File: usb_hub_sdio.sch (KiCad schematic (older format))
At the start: 18 parts, among them U901 USB2660, Y901 24MHz

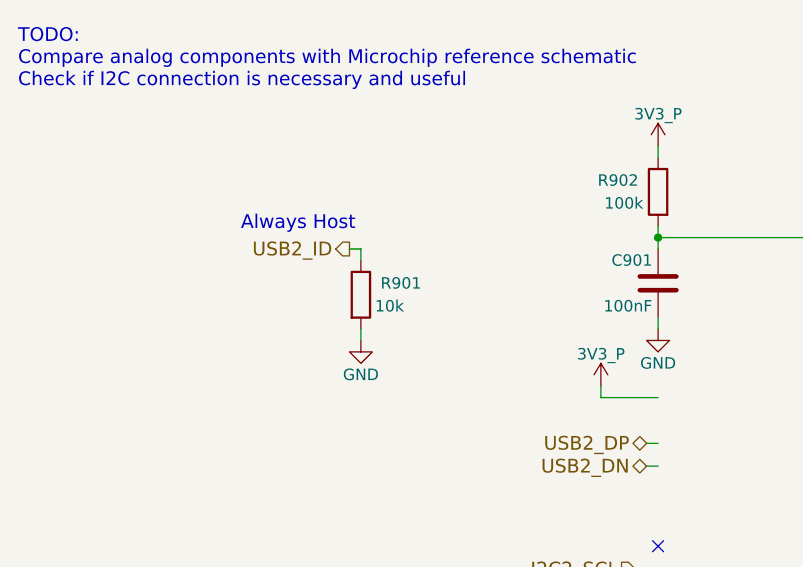
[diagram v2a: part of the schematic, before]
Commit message: Begin assigning footprints to passive components, add component information to the common 10k resistors throughout the schematic, include TVS diodes on the switch/button I/O pins, use the DB2J20900L schottky diode throughout the design (in place of the ZLLS400)
Added notes about the battery holder, battery size, and the fact that the 103HT thermistor can fit underneath the 18650 battery when the battery is insterted into the holder.

Included frequency response curve for the new/cheaper SMD speaker (slightly thicker mechanical dimension).

Included note about the RedPine RS9116's SDIO_RESET# line expecting a 2.31V VIH logic level, increased the pull-up to 100k (M.2 standard states that this is should be 1.8V level).

Added a TODO note stating the 1.8V logic-level I2C devices should share the same level-shifter that will be on the top-level circuit (in next commit).
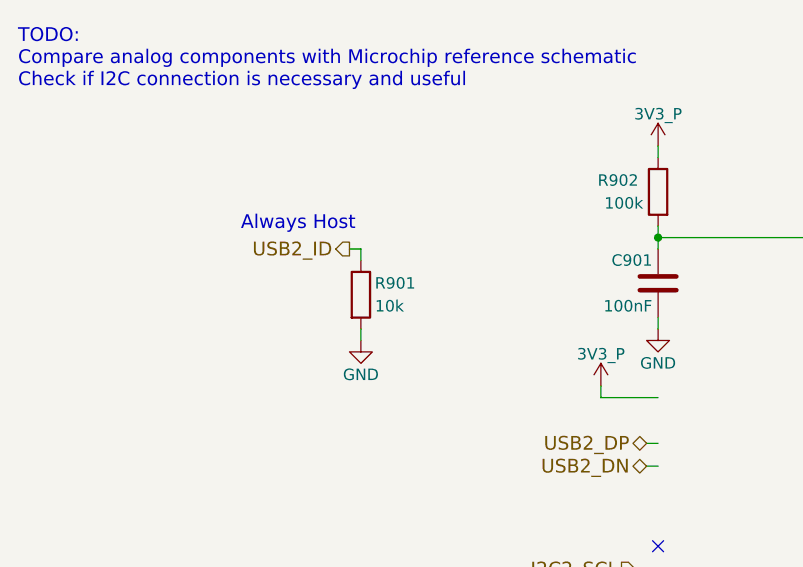
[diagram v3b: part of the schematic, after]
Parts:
- R901: footprint (none) -> Resistors_SMD:R_0603; Distrib Link (none) -> https://www.digikey.com/product-detail/en/stackpole-electro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; Distrib PN (none) -> RMCF0603JG10K0CT-ND; MFG Name (none) -> Stackpole; MFG Part Num (none) -> RMCF0603JG10K0; Others (none) -> https://www.digikey.com/products/en/resistors/chip-resistor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; Tolerance (none) -> 5%
- R902, R903: footprint (none) -> Resistors_SMD:R_0603
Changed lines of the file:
@@
 F 0 "R903" H 5075 5950 50  0000 C CNN
 F 1 "12k" H 5025 6050 50  0000 C CNN
-F 2 "" V 4830 6000 50  0001 C CNN
+F 2 "Resistors_SMD:R_0603" V 4830 6000 50  0001 C CNN
 F 3 "" H 4900 6000 50  0001 C CNN
 	1    4900 6000
@@
 $EndComp
 $Comp
-L GND #PWR905
+L GND #PWR0138
 U 1 1 5AFD409A
 P 4250 6550
-F 0 "#PWR905" H 4250 6300 50  0001 C CNN
+F 0 "#PWR0138" H 4250 6300 50  0001 C CNN
 F 1 "GND" H 4250 6400 50  0000 C CNN
 F 2 "" H 4250 6550 50  0001 C CNN
@@
 $EndComp
 $Comp
-L GND #PWR906
+L GND #PWR0139
 U 1 1 5AFD422F
 P 4650 6550
-F 0 "#PWR906" H 4650 6300 50  0001 C CNN
+F 0 "#PWR0139" H 4650 6300 50  0001 C CNN
 F 1 "GND" H 4650 6400 50  0000 C CNN
 F 2 "" H 4650 6550 50  0001 C CNN
@@
 F 0 "R902" H 4075 1700 50  0000 C CNN
 F 1 "100k" H 4050 1600 50  0000 C CNN
-F 2 "" V 3830 1650 50  0001 C CNN
+F 2 "Resistors_SMD:R_0603" V 3830 1650 50  0001 C CNN
 F 3 "" H 3900 1650 50  0001 C CNN
 	1    3900 1650
@@
 $EndComp
 $Comp
-L GND #PWR904
+L GND #PWR0140
 U 1 1 5AE5E881
 P 3900 2250
-F 0 "#PWR904" H 3900 2000 50  0001 C CNN
+F 0 "#PWR0140" H 3900 2000 50  0001 C CNN
 F 1 "GND" H 3900 2100 50  0000 C CNN
 F 2 "" H 3900 2250 50  0001 C CNN
@@
 $EndComp
 $Comp
-L 3V3_P #PWR903
+L 3V3_P #PWR0141
 U 1 1 5AE604F2
 P 3900 1450
-F 0 "#PWR903" H 3900 1300 50  0001 C CNN
+F 0 "#PWR0141" H 3900 1300 50  0001 C CNN
 F 1 "3V3_P" H 3900 1590 50  0000 C CNN
 F 2 "" H 3900 1450 50  0001 C CNN
@@
 USB2_ID
 $Comp
-L R R901
-U 1 1 5AF23335
-P 2600 2100
-F 0 "R901" H 2775 2150 50  0000 C CNN
-F 1 "10k" H 2725 2050 50  0000 C CNN
-F 2 "" V 2530 2100 50  0001 C CNN
-F 3 "" H 2600 2100 50  0001 C CNN
-	1    2600 2100
-	1    0    0    -1
-$EndComp
-$Comp
-L GND #PWR901
+L GND #PWR0142
 U 1 1 5AF52101
 P 2600 2300
-F 0 "#PWR901" H 2600 2050 50  0001 C CNN
+F 0 "#PWR0142" H 2600 2050 50  0001 C CNN
 F 1 "GND" H 2600 2150 50  0000 C CNN
 F 2 "" H 2600 2300 50  0001 C CNN
@@
 $EndComp
 $Comp
-L GND #PWR908
+L GND #PWR0143
 U 1 1 5B0063B4
 P 4900 6200
-F 0 "#PWR908" H 4900 5950 50  0001 C CNN
+F 0 "#PWR0143" H 4900 5950 50  0001 C CNN
 F 1 "GND" H 4900 6050 50  0000 C CNN
 F 2 "" H 4900 6200 50  0001 C CNN
@@
 $EndComp
 $Comp
-L GND #PWR910
+L GND #PWR0144
 U 1 1 5B00652F
 P 6300 5900
-F 0 "#PWR910" H 6300 5650 50  0001 C CNN
+F 0 "#PWR0144" H 6300 5650 50  0001 C CNN
 F 1 "GND" H 6300 5750 50  0000 C CNN
 F 2 "" H 6300 5900 50  0001 C CNN
@@
 NoConn ~ 3900 3500
 $Comp
-L 3V3_P #PWR909
+L 3V3_P #PWR0145
 U 1 1 5B00782B
 P 5700 950
-F 0 "#PWR909" H 5700 800 50  0001 C CNN
+F 0 "#PWR0145" H 5700 800 50  0001 C CNN
 F 1 "3V3_P" H 5700 1090 50  0000 C CNN
 F 2 "" H 5700 950 50  0001 C CNN
@@
 $EndComp
 $Comp
-L GND #PWR907
+L GND #PWR0146
 U 1 1 5B008B68
 P 4700 1450
-F 0 "#PWR907" H 4700 1200 50  0001 C CNN
+F 0 "#PWR0146" H 4700 1200 50  0001 C CNN
 F 1 "GND" H 4700 1300 50  0000 C CNN
 F 2 "" H 4700 1450 50  0001 C CNN
@@
 $EndComp
 $Comp
-L GND #PWR912
+L GND #PWR0147
 U 1 1 5B00B145
 P 7600 2150
-F 0 "#PWR912" H 7600 1900 50  0001 C CNN
+F 0 "#PWR0147" H 7600 1900 50  0001 C CNN
 F 1 "GND" H 7600 2000 50  0000 C CNN
 F 2 "" H 7600 2150 50  0001 C CNN
@@
 $EndComp
 $Comp
-L GND #PWR911
+L GND #PWR0148
 U 1 1 5B00BA9D
 P 7600 1450
-F 0 "#PWR911" H 7600 1200 50  0001 C CNN
+F 0 "#PWR0148" H 7600 1200 50  0001 C CNN
 F 1 "GND" H 7600 1300 50  0000 C CNN
 F 2 "" H 7600 1450 50  0001 C CNN
@@
 uSD_DATA3
 $Comp
-L 3V3_P #PWR902
+L 3V3_P #PWR0149
 U 1 1 5B00E09B
 P 3650 2500
-F 0 "#PWR902" H 3650 2350 50  0001 C CNN
+F 0 "#PWR0149" H 3650 2350 50  0001 C CNN
 F 1 "3V3_P" H 3650 2640 50  0000 C CNN
 F 2 "" H 3650 2500 50  0001 C CNN
@@
 	5200 1350 5200 1400
 Connection ~ 4700 1400
+$Comp
+L R R901
+U 1 1 5B31F267
+P 2600 2100
+F 0 "R901" H 2750 2150 50  0000 C CNN
+F 1 "10k" H 2725 2050 50  0000 C CNN
+F 2 "Resistors_SMD:R_0603" V 2530 2100 50  0001 C CNN
+F 3 "https://www.seielect.com/Catalog/SEI-RMCF_RMCP.pdf" H 2600 2100 50  0001 C CNN
+F 4 "Stackpole" H 2600 2100 60  0001 C CNN "MFG Name"
+F 5 "RMCF0603JG10K0" H 2600 2100 60  0001 C CNN "MFG Part Num"
+F 6 "RMCF0603JG10K0CT-ND" H 2600 2100 60  0001 C CNN "Distrib PN"
+F 7 "https://www.digikey.com/product-detail/en/stackpole-electronics-inc/RMCF0603JG10K0/RMCF0603JG10K0CT-ND/4425128" H 2600 2100 60  0001 C CNN "Distrib Link"
+F 8 "5%" H 2600 2100 60  0001 C CNN "Tolerance"
+F 9 "https://www.digikey.com/products/en/resistors/chip-resistor-surface-mount/52?FV=ffe00034%2C400005%2C1f140000%2Cmu10+kOhms%7C2085&quantity=&ColumnSort=1000011&page=1&pageSize=500" H 2600 2100 60  0001 C CNN "Others"
+	1    2600 2100
+	1    0    0    -1
+$EndComp
 $EndSCHEMATC

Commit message: Move MIPI DSI & CSI sheets into a "MIPI" sheet, both DSI and CSI will likely use the I2C level shifter
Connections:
- net labels added: I2C1_SCL, I2C1_SDA
- net labels removed: I2C2_SCL, I2C2_SDA
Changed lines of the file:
@@
 $Descr A4 11693 8268
 encoding utf-8
-Sheet 9 21
+Sheet 9 22
 Title ""
 Date "2018-05-18"
@@
 USB2_DP
 Text HLabel 3800 3300 0    60   Input ~ 0
-I2C2_SCL
+I2C1_SCL
 Text HLabel 3800 3400 0    60   BiDi ~ 0
-I2C2_SDA
+I2C1_SDA
 Text HLabel 2550 1900 0    60   Output ~ 0
 USB2_ID

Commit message: Add Prolific MA8627 USB hub + SDIO bridge chip and use it in place of the USB2660, SD interface used with the uSD (not WLAN)
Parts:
- removed U901: USB2660, symbol USB2660
- added Q901: DMG2301L, symbol Q_PMOS_GSD
- added R904, R905: 0, Resistors_SMD:R_0603, symbol R
- added R906: 10k, symbol R
- added R907: 330, Resistors_SMD:R_0603, symbol R
- added R908, R909, R910, R911: NC, Resistors_SMD:R_0603, symbol R
- added U901: MA8627, symbol MA8627
- C901: value 100nF -> 4.7uF
- C902, C903: value NC -> 18pF; footprint (none) -> Capacitors_SMD:C_0603
- C904: value 1uF -> 100nF
- C905: value 1nF -> 10uF; footprint (none) -> Resistors_SMD:R_0603
- C906, C907: value 4.7uF -> 10uF; footprint (none) -> Resistors_SMD:R_0603
- C908: value 1uF -> 10uF; footprint (none) -> Resistors_SMD:R_0603
- C909: footprint (none) -> Capacitors_SMD:C_0603
- C910, C911: value 1nF -> 10uF; footprint (none) -> Capacitors_SMD:C_0603
- C912: value 100nF -> NC; footprint (none) -> Capacitors_SMD:C_0603
- C913: value 100nF -> 10uF; footprint (none) -> Capacitors_SMD:C_0603
- R902: value 100k -> NC
- R903: value 12k -> 330
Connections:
- net labels added: 3V3_SD, 5V_P, CD, DM0, DP0, HV33, RDRV18, RDRV33, RDRV5, SDCD, SMARTCARD_DM, SMARTCARD_DP, SRST, WP
- net labels removed: 3V3_P, I2C1_SCL, I2C1_SDA
- wire segments 76 -> 116
- no-connect marks 32 -> 5
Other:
- note added: "Can be swapped arround depending on layout"
- note added: "TODO:\nShould be NC?"
- note added: "≤1%"
- note removed: "18pF"
- note removed: "TODO:\nCompare analog components with Microchip reference schematic\nCheck if I2C connection is necessary and useful"
- moved on the sheet: C902, C903, R901, Y901

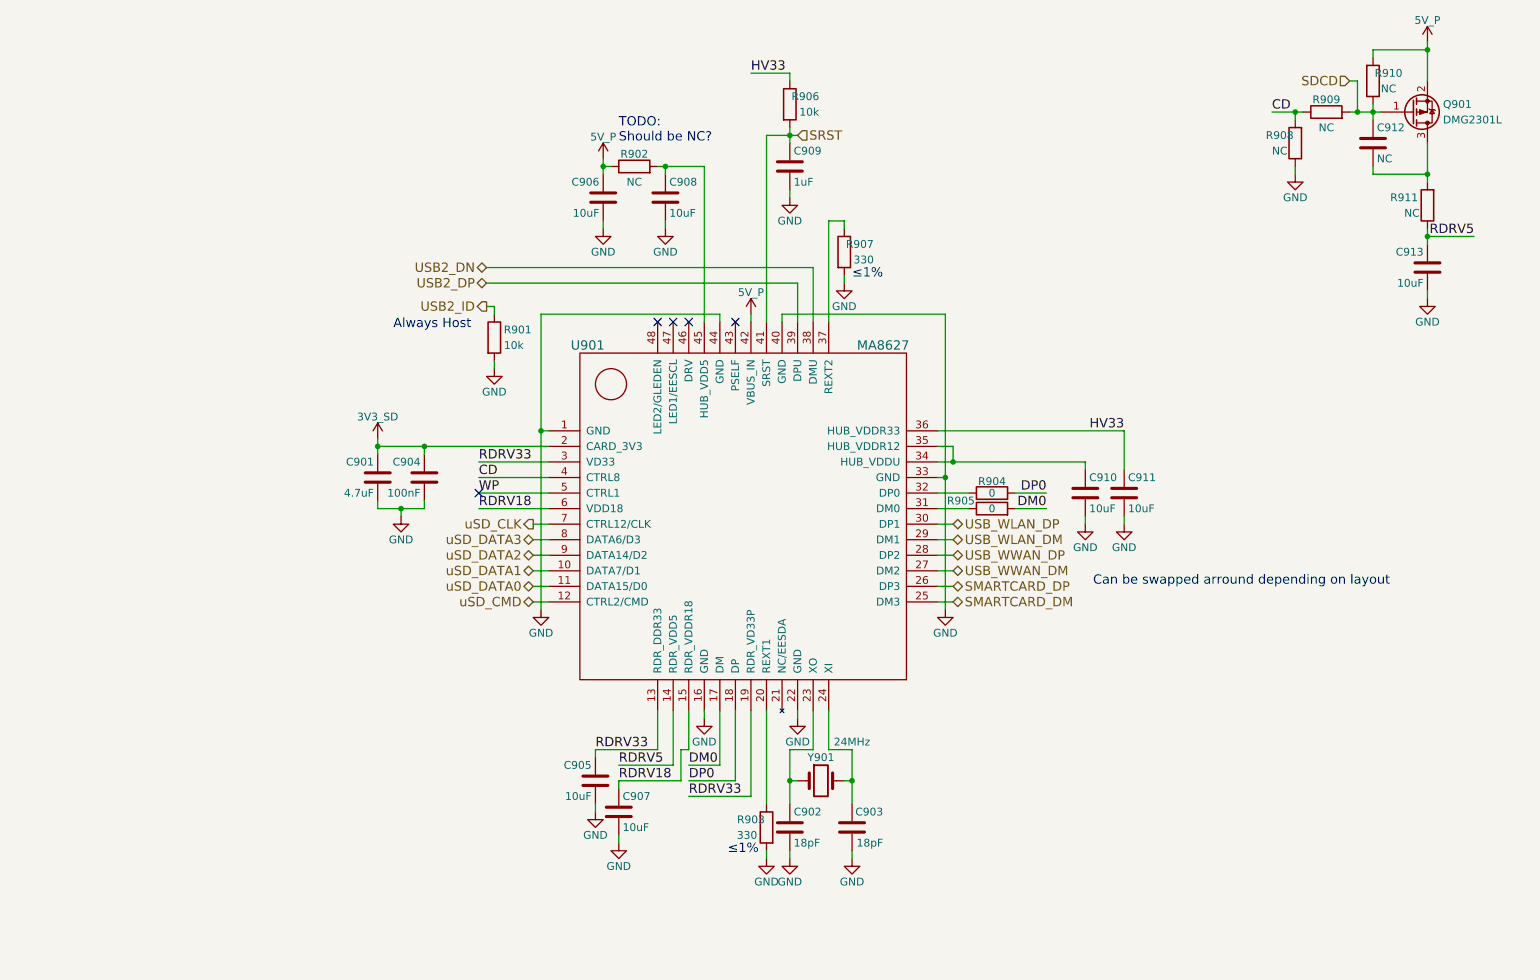
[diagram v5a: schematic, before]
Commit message: Add smart card circuit using the SEC1110 USB to ISO/IEC 7816 bridge chip, include ID-0001/2FF/mini-SIM socket connector selection informatino (1010027182)
Need to create footprint for the mini-SIM socket
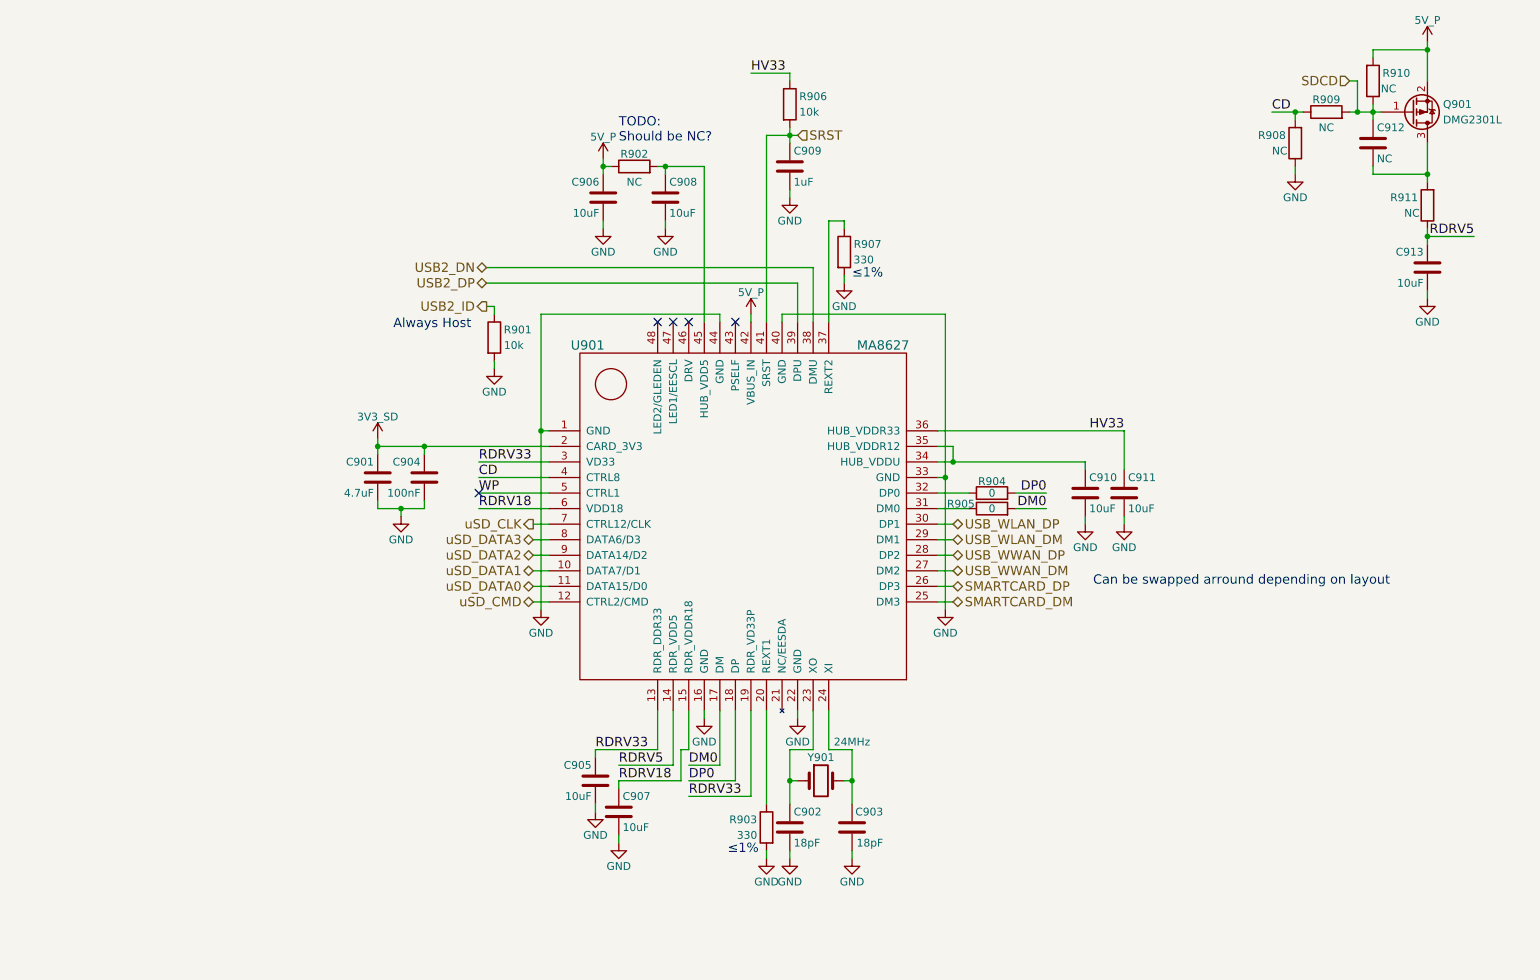
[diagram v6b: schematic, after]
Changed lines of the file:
@@
 $Descr A4 11693 8268
 encoding utf-8
-Sheet 9 22
+Sheet 9 23
 Title ""
-Date "2018-05-18"
+Date "2018-05-23"
 Rev "v0.1.0"
 Comp "Purism SPC"
@@
 U 1 1 5B07DA80
 P 7400 3800
-F 0 "R905" V 7450 4000 50  0000 C CNN
+F 0 "R905" V 7430 4000 50  0000 C CNN
 F 1 "0" V 7400 3800 50  0000 C CNN
 F 2 "Resistors_SMD:R_0603" V 7330 3800 50  0001 C CNN
@@
 U 1 1 5B09B6A4
 P 9350 1450
-F 0 "R908" H 9450 1400 50  0000 C CNN
+F 0 "R908" H 9500 1400 50  0000 C CNN
 F 1 "NC" H 9450 1500 50  0000 C CNN
 F 2 "Resistors_SMD:R_0603" V 9280 1450 50  0001 C CNN
@@
 U 1 1 5B09C779
 P 9850 1050
-F 0 "R910" H 9950 1000 50  0000 C CNN
+F 0 "R910" H 10000 1000 50  0000 C CNN
 F 1 "NC" H 9950 1100 50  0000 C CNN
 F 2 "Resistors_SMD:R_0603" V 9780 1050 50  0001 C CNN
@@
 U 1 1 5B0FC98F
 P 6100 1200
-F 0 "R906" H 6200 1250 50  0000 C CNN
+F 0 "R906" H 6250 1250 50  0000 C CNN
 F 1 "10k" H 6225 1150 50  0000 C CNN
 F 2 "" V 6030 1200 50  0001 C CNN
@@
 U 1 1 5B101B57
 P 5950 5850
-F 0 "R903" H 6050 5900 50  0000 C CNN
+F 0 "R903" H 6100 5900 50  0000 C CNN
 F 1 "330" H 6075 5800 50  0000 C CNN
 F 2 "Resistors_SMD:R_0603" V 5880 5850 50  0001 C CNN
@@
 U 1 1 5B10A19C
 P 6450 2150
-F 0 "R907" H 6550 2200 50  0000 C CNN
+F 0 "R907" H 6600 2200 50  0000 C CNN
 F 1 "330" H 6575 2100 50  0000 C CNN
 F 2 "Resistors_SMD:R_0603" V 6380 2150 50  0001 C CNN

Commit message: Make changes to the USB hub + SD bridge circuit and uSD sheet based on Prolific's feedback after asking questions
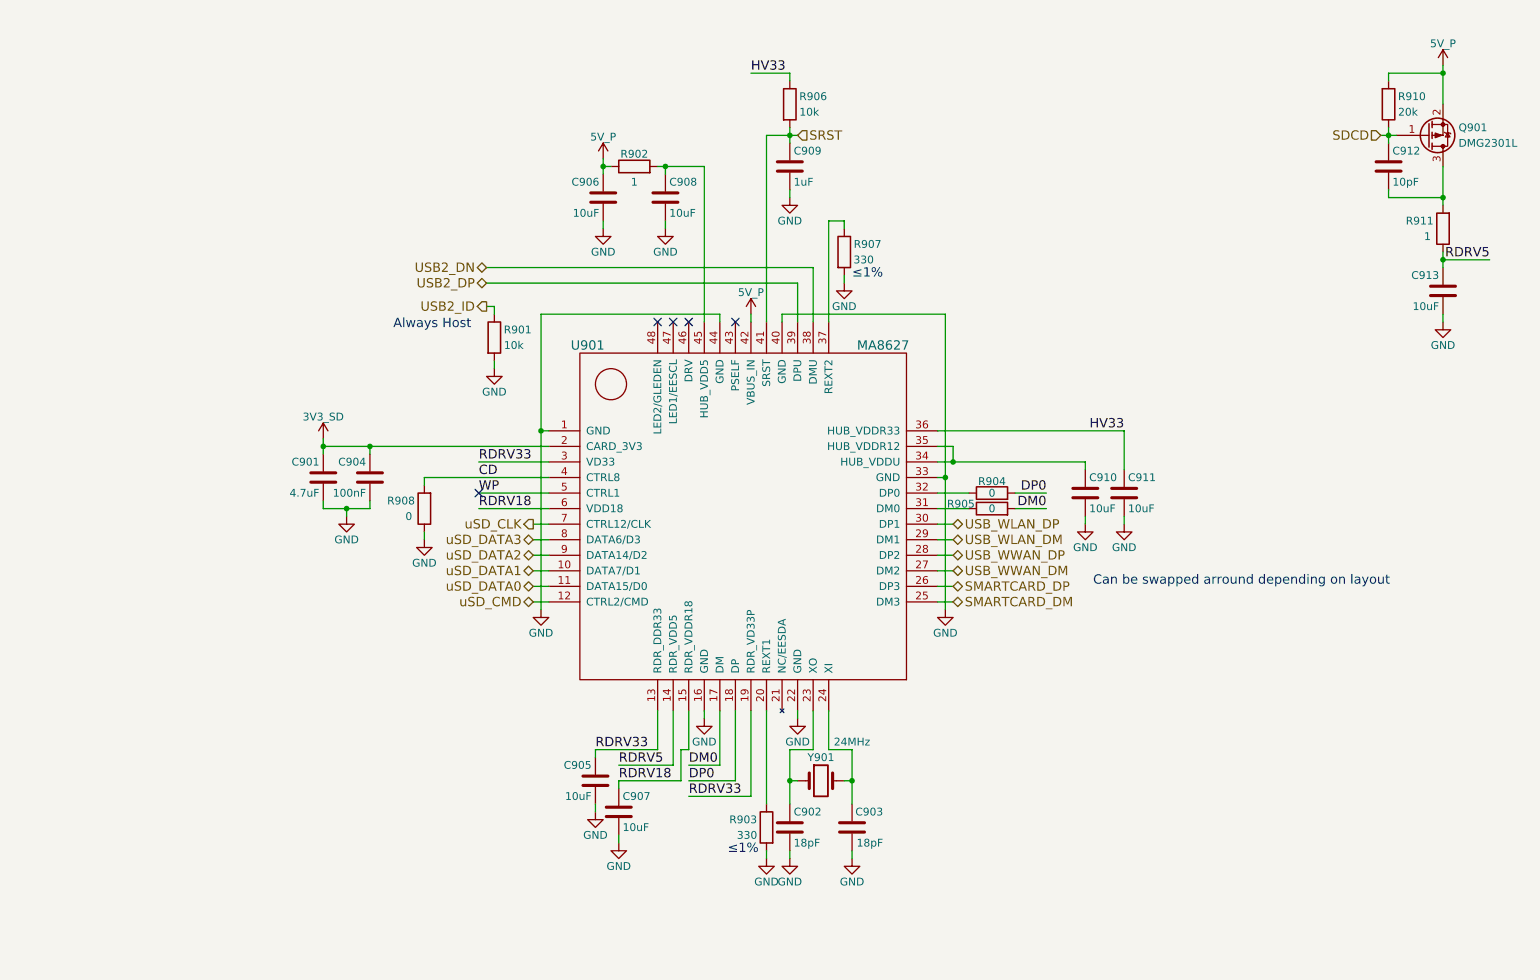
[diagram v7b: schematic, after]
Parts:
- removed R909: NC, Resistors_SMD:R_0603, symbol R
- C912: value NC -> 10pF
- R902, R911: value NC -> 1
- R908: value NC -> 0
- R910: value NC -> 20k
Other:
- note removed: "TODO:\nShould be NC?"
- moved on the sheet: C901, C904, C912, C913, Q901, R908, R910, R911
